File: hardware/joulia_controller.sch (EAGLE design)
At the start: 27 parts, among them IC1 LM2902D, IC2 LM2902D, U1 MMBT2222ALT1G, U2 MMBT2222ALT1G

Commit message: Increasing power trace width and adding input resistors to transistors.
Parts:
- added R16, R9: 1K, resistor:R-US_R0402
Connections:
- new net N$15: R9.1, U1.B
- new net N$16: R16.1, U2.B
- net HEOUT: now also R9.2; no longer U1.B
- net PPOUT: now also R16.2; no longer U2.B
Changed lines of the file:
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@@
 <?xml version="1.0" encoding="utf-8"?>
 <!DOCTYPE eagle SYSTEM "eagle.dtd">
-<eagle version="7.2.0">
+<eagle version="8.0.1">
 <drawing>
 <settings>
@@
 <part name="SUPPLY15" library="supply2" deviceset="GND" device=""/>
 <part name="SUPPLY16" library="supply2" deviceset="GND" device=""/>
+<part name="R9" library="resistor" deviceset="R-US_" device="R0402" value="1K"/>
+<part name="R16" library="resistor" deviceset="R-US_" device="R0402" value="1K"/>
 </parts>
 <sheets>
@@
 <instance part="SUPPLY15" gate="GND" x="50.8" y="81.28"/>
 <instance part="SUPPLY16" gate="GND" x="50.8" y="17.78"/>
+<instance part="R9" gate="G$1" x="190.5" y="109.22" rot="R180"/>
+<instance part="R16" gate="G$1" x="190.5" y="86.36" rot="R180"/>
 </instances>
 <busses>
@@
 <net name="HEOUT" class="0">
 <segment>
-<pinref part="U1" gate="A" pin="B"/>
-<wire x1="198.12" y1="109.22" x2="193.04" y2="109.22" width="0.1524" layer="91"/>
-<label x="193.04" y="109.22" size="1.778" layer="95"/>
-</segment>
-<segment>
 <pinref part="PI" gate="A" pin="13"/>
 <wire x1="-78.74" y1="91.44" x2="-96.52" y2="91.44" width="0.1524" layer="91"/>
 <label x="-96.52" y="91.44" size="1.778" layer="95"/>
 </segment>
+<segment>
+<pinref part="R9" gate="G$1" pin="2"/>
+<label x="180.34" y="109.22" size="1.778" layer="95"/>
+<wire x1="185.42" y1="109.22" x2="180.34" y2="109.22" width="0.1524" layer="91"/>
+</segment>
 </net>
 <net name="PPOUT" class="0">
-<segment>
-<pinref part="U2" gate="A" pin="B"/>
-<wire x1="198.12" y1="86.36" x2="193.04" y2="86.36" width="0.1524" layer="91"/>
-<label x="193.04" y="86.36" size="1.778" layer="95"/>
-</segment>
 <segment>
 <pinref part="PI" gate="A" pin="11"/>
@@
 <label x="-96.52" y="93.98" size="1.778" layer="95"/>
 </segment>
-</net>
+<segment>
+<pinref part="R16" gate="G$1" pin="2"/>
+<label x="180.34" y="86.36" size="1.778" layer="95"/>
+<wire x1="185.42" y1="86.36" x2="180.34" y2="86.36" width="0.1524" layer="91"/>
+</segment>
+</net>
+<net name="N$15" class="0">
+<segment>
+<pinref part="U1" gate="A" pin="B"/>
+<pinref part="R9" gate="G$1" pin="1"/>
+<wire x1="195.58" y1="109.22" x2="198.12" y2="109.22" width="0.1524" layer="91"/>
+</segment>
+</net>
+<net name="N$16" class="0">
+<segment>
+<pinref part="U2" gate="A" pin="B"/>
+<pinref part="R16" gate="G$1" pin="1"/>
+<wire x1="195.58" y1="86.36" x2="198.12" y2="86.36" width="0.1524" layer="91"/>
+</segment>
+</net>

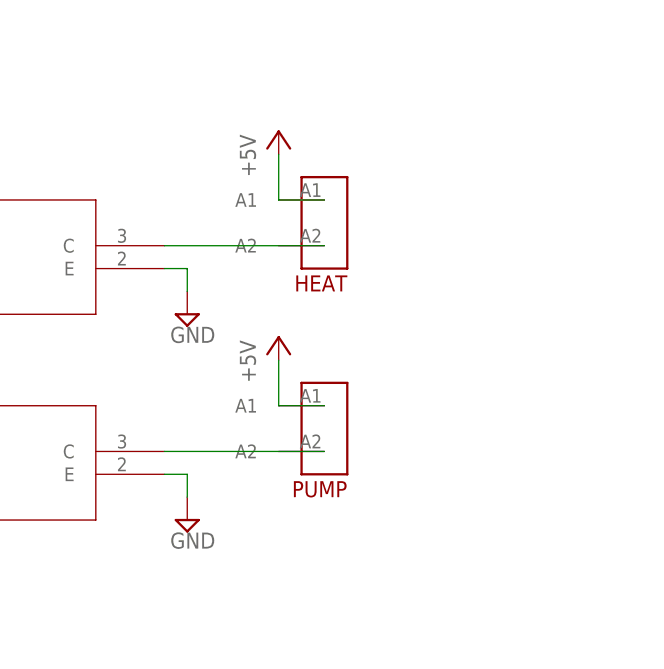
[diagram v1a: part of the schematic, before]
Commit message: Adding Triac and Heatsink
Need opto-isolation and power terminals.
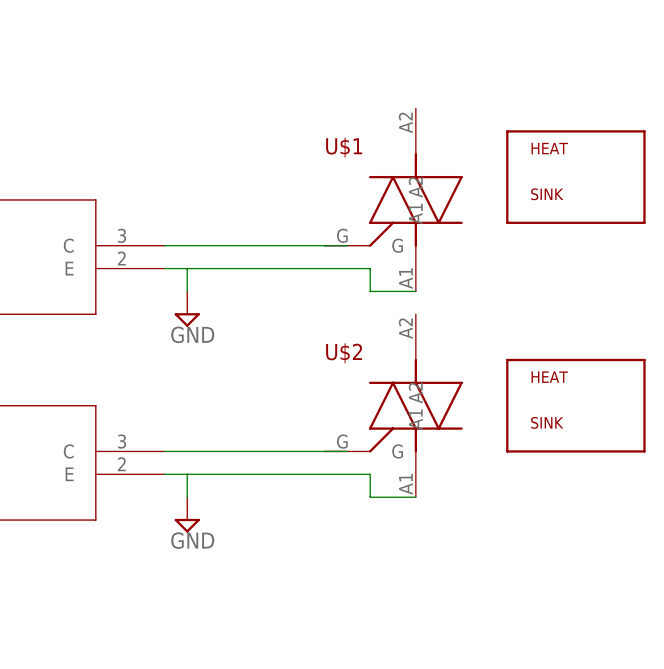
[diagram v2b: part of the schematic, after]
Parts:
- removed HEAT, PUMP: MTA-100-2HDR2, digikey:MTA-100-2HDR2
- added U$1, U$2: T3050H-6I, digikey:T3050H-6I
- added U$3, U$4: VM1-038-1AE, digikey:VM1-038-1AE
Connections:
- net +5V: no longer HEAT.A1, PUMP.A1
- net GND: now also U$1.A1, U$2.A1
- net N$13: now also U$1.G; no longer HEAT.A2
- net N$14: now also U$2.G; no longer PUMP.A2
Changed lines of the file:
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@@
 <part name="U1" library="digikey" deviceset="MMBT2222ALT1G" device=""/>
 <part name="U2" library="digikey" deviceset="MMBT2222ALT1G" device=""/>
-<part name="HEAT" library="digikey" deviceset="MTA-100-2" device="HDR2"/>
-<part name="PUMP" library="digikey" deviceset="MTA-100-2" device="HDR2"/>
-<part name="P+1" library="supply1" deviceset="+5V" device=""/>
-<part name="P+2" library="supply1" deviceset="+5V" device=""/>
 <part name="SUPPLY10" library="supply2" deviceset="GND" device=""/>
 <part name="SUPPLY11" library="supply2" deviceset="GND" device=""/>
@@
 <part name="R9" library="resistor" deviceset="R-US_" device="R0402" value="1K"/>
 <part name="R16" library="resistor" deviceset="R-US_" device="R0402" value="1K"/>
+<part name="U$1" library="digikey" deviceset="T3050H-6I" device=""/>
+<part name="U$2" library="digikey" deviceset="T3050H-6I" device=""/>
+<part name="U$3" library="digikey" deviceset="VM1-038-1AE" device=""/>
+<part name="U$4" library="digikey" deviceset="VM1-038-1AE" device=""/>
 </parts>
 <sheets>
@@
 <instance part="U1" gate="A" x="198.12" y="109.22"/>
 <instance part="U2" gate="A" x="198.12" y="86.36"/>
-<instance part="HEAT" gate="A" x="261.62" y="111.76" rot="MR0"/>
-<instance part="PUMP" gate="A" x="261.62" y="88.9" rot="MR0"/>
-<instance part="P+1" gate="1" x="256.54" y="121.92"/>
-<instance part="P+2" gate="1" x="256.54" y="99.06"/>
 <instance part="SUPPLY10" gate="GND" x="246.38" y="78.74"/>
 <instance part="SUPPLY11" gate="GND" x="246.38" y="101.6"/>
@@
 <instance part="R9" gate="G$1" x="190.5" y="109.22" rot="R180"/>
 <instance part="R16" gate="G$1" x="190.5" y="86.36" rot="R180"/>
+<instance part="U$1" gate="G$1" x="269.24" y="114.3"/>
+<instance part="U$2" gate="G$1" x="269.24" y="91.44"/>
+<instance part="U$3" gate="G$1" x="289.56" y="116.84"/>
+<instance part="U$4" gate="G$1" x="289.56" y="91.44"/>
 </instances>
 <busses>
@@
 <wire x1="243.84" y1="106.68" x2="246.38" y2="106.68" width="0.1524" layer="91"/>
 <wire x1="246.38" y1="106.68" x2="246.38" y2="104.14" width="0.1524" layer="91"/>
+<wire x1="246.38" y1="106.68" x2="266.7" y2="106.68" width="0.1524" layer="91"/>
+<wire x1="266.7" y1="106.68" x2="266.7" y2="104.14" width="0.1524" layer="91"/>
+<pinref part="U$1" gate="G$1" pin="A1"/>
+<wire x1="266.7" y1="104.14" x2="271.78" y2="104.14" width="0.1524" layer="91"/>
 </segment>
 <segment>
@@
 <wire x1="243.84" y1="83.82" x2="246.38" y2="83.82" width="0.1524" layer="91"/>
 <wire x1="246.38" y1="83.82" x2="246.38" y2="81.28" width="0.1524" layer="91"/>
+<wire x1="246.38" y1="83.82" x2="266.7" y2="83.82" width="0.1524" layer="91"/>
+<wire x1="266.7" y1="83.82" x2="266.7" y2="81.28" width="0.1524" layer="91"/>
+<pinref part="U$2" gate="G$1" pin="A1"/>
+<wire x1="266.7" y1="81.28" x2="271.78" y2="81.28" width="0.1524" layer="91"/>
 </segment>
 <segment>
@@
 </segment>
 <segment>
-<pinref part="P+1" gate="1" pin="+5V"/>
-<wire x1="256.54" y1="119.38" x2="256.54" y2="114.3" width="0.1524" layer="91"/>
-<pinref part="HEAT" gate="A" pin="A1"/>
-<wire x1="256.54" y1="114.3" x2="261.62" y2="114.3" width="0.1524" layer="91"/>
-</segment>
-<segment>
-<pinref part="P+2" gate="1" pin="+5V"/>
-<wire x1="256.54" y1="96.52" x2="256.54" y2="91.44" width="0.1524" layer="91"/>
-<pinref part="PUMP" gate="A" pin="A1"/>
-<wire x1="256.54" y1="91.44" x2="261.62" y2="91.44" width="0.1524" layer="91"/>
-</segment>
-<segment>
 <pinref part="P+3" gate="1" pin="+5V"/>
 <wire x1="-71.12" y1="38.1" x2="-71.12" y2="33.02" width="0.1524" layer="91"/>
@@
 <segment>
 <pinref part="U1" gate="A" pin="C"/>
-<wire x1="261.62" y1="109.22" x2="243.84" y2="109.22" width="0.1524" layer="91"/>
-<pinref part="HEAT" gate="A" pin="A2"/>
+<pinref part="U$1" gate="G$1" pin="G"/>
+<wire x1="243.84" y1="109.22" x2="261.62" y2="109.22" width="0.1524" layer="91"/>
+<wire x1="264.16" y1="109.22" x2="261.62" y2="109.22" width="0.1524" layer="91"/>
 </segment>
 </net>
@@
 <segment>
 <pinref part="U2" gate="A" pin="C"/>
+<pinref part="U$2" gate="G$1" pin="G"/>
 <wire x1="243.84" y1="86.36" x2="261.62" y2="86.36" width="0.1524" layer="91"/>
-<pinref part="PUMP" gate="A" pin="A2"/>
-</segment>
-</net>
+<wire x1="264.16" y1="86.36" x2="261.62" y2="86.36" width="0.1524" layer="91"/>
+</segment>
+</net>

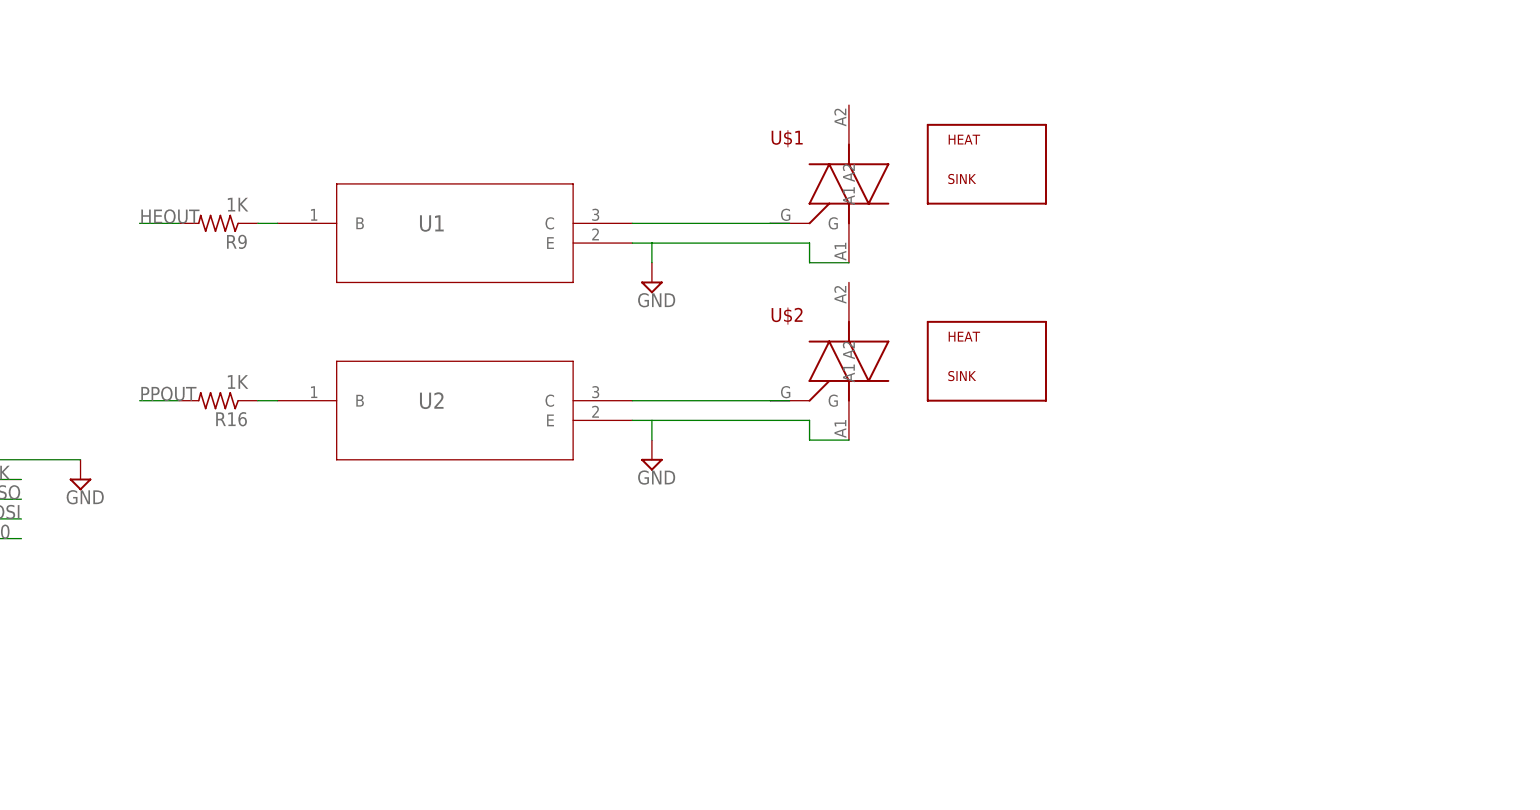
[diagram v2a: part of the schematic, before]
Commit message: Adding connectors and SSR to board
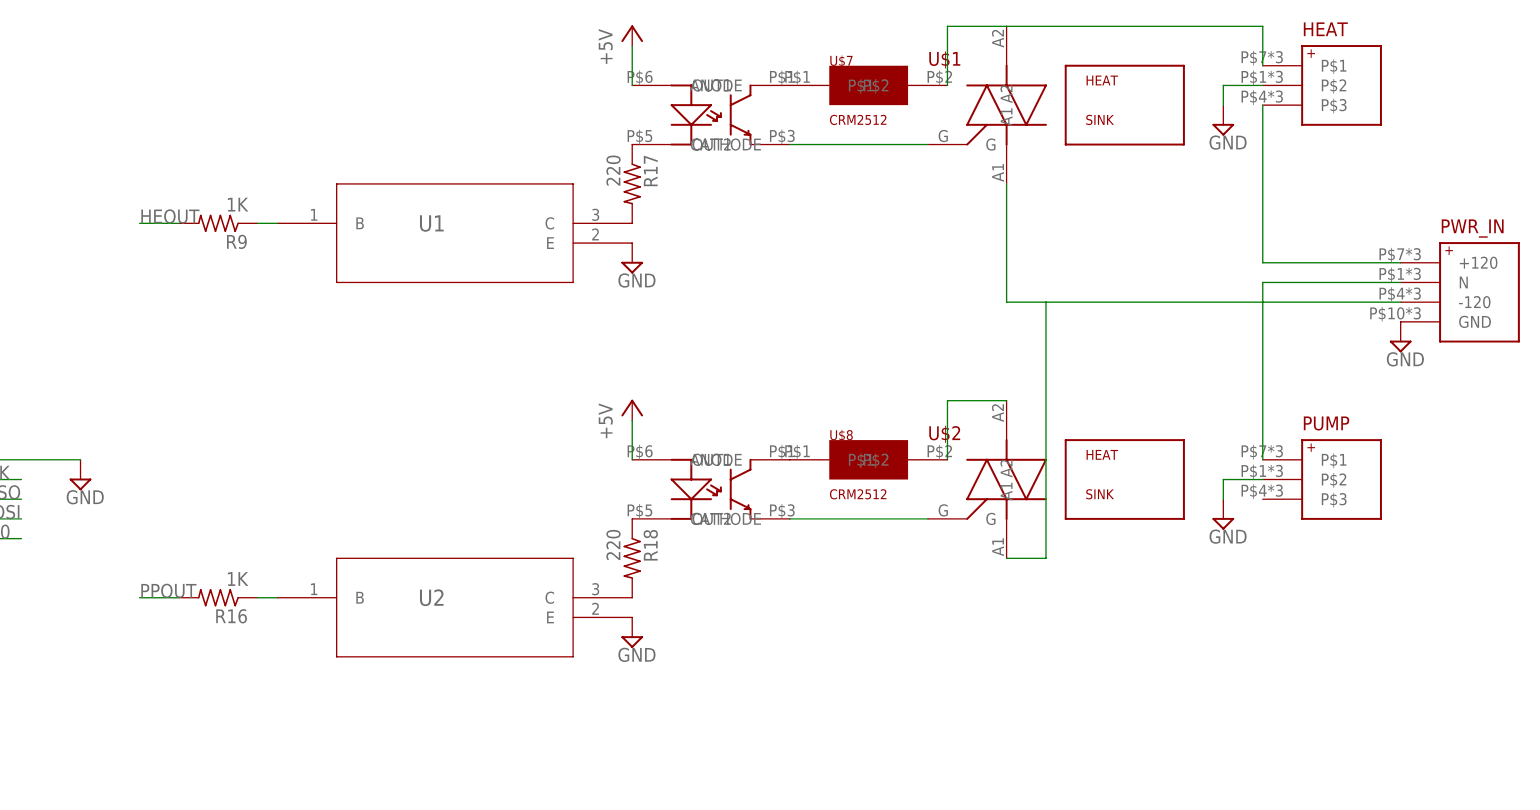
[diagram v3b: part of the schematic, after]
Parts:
- added HEAT, PUMP: PC1720589, digikey:PC1720589
- added PWR_IN: PC1720592, digikey:PC1720592
- added R17, R18: 220, resistor:R-US_R0402
- added U$5, U$6: MOC3020S, digikey:MOC3020S
- added U$7, U$8: CRM2512, digikey:CRM2512
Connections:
- new net N$17: R18.2, U2.C
- new net N$18: R18.1, U$6.CATHODE
- new net N$19: U$1.G, U$5.OUT2
- new net N$20: U$5.OUT1, U$7.P$1
- new net N$21: U$6.OUT1, U$8.P$1
- new net N$22: HEAT.P$1, U$1.A2, U$7.P$2
- new net N$23: U$2.G, U$6.OUT2
- new net N$24: U$2.A2, U$8.P$2
- new net N$25: HEAT.P$3, PWR_IN.+120
- new net N$26: PWR_IN.-120, U$1.A1, U$2.A1
- new net N$27: PUMP.P$1, PWR_IN.N
- net +5V: now also U$5.ANODE, U$6.ANODE
- net GND: now also HEAT.P$2, PUMP.P$2, PWR_IN.GND; no longer U$1.A1, U$2.A1
- net N$13: now also R17.2; no longer U$1.G
- net N$14: now also R17.1, U$5.CATHODE; no longer U$2.G, U2.C
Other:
- moved on the sheet: R16, U$1, U$2, U2

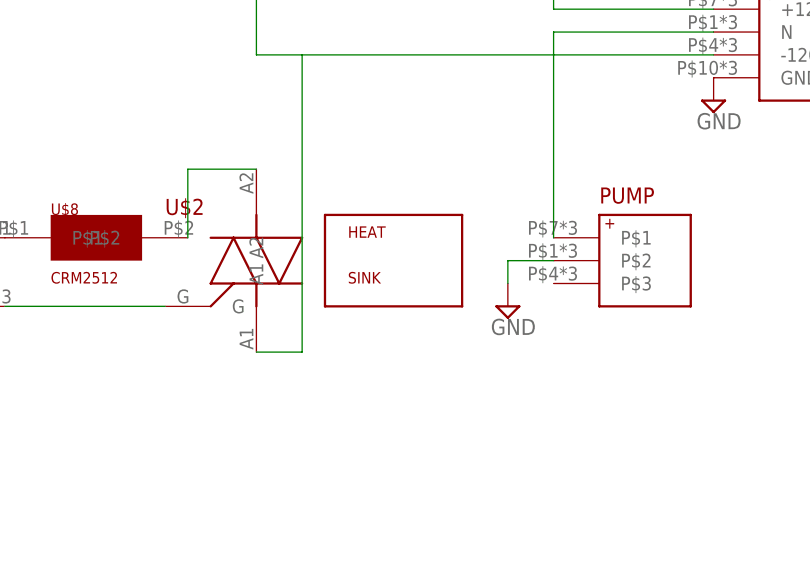
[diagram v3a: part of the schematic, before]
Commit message: Routing and rearrangement for power
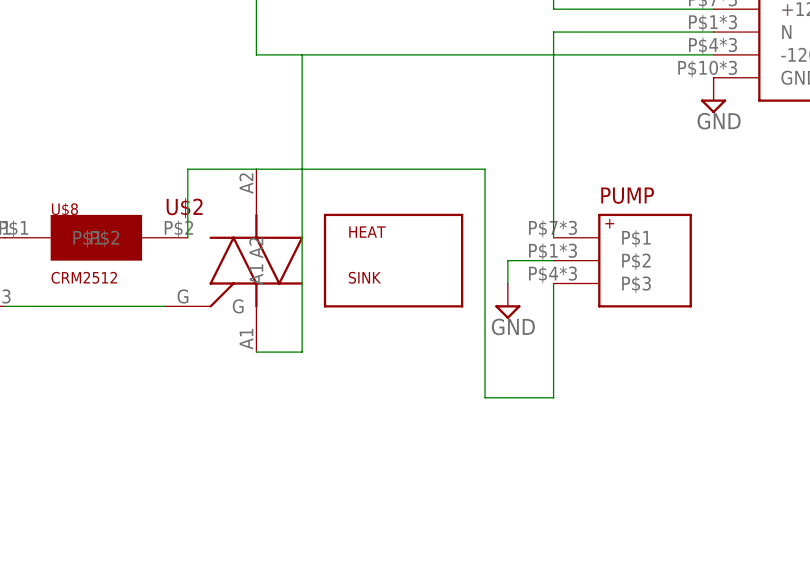
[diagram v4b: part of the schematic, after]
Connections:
- net N$24: now also PUMP.P$3
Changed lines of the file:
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@@
 <pinref part="U$2" gate="G$1" pin="A2"/>
 <wire x1="284.48" y1="86.36" x2="292.1" y2="86.36" width="0.1524" layer="91"/>
+<wire x1="292.1" y1="86.36" x2="317.5" y2="86.36" width="0.1524" layer="91"/>
+<wire x1="317.5" y1="86.36" x2="317.5" y2="60.96" width="0.1524" layer="91"/>
+<pinref part="PUMP" gate="G$1" pin="P$3"/>
+<wire x1="317.5" y1="60.96" x2="325.12" y2="60.96" width="0.1524" layer="91"/>
+<wire x1="325.12" y1="60.96" x2="325.12" y2="73.66" width="0.1524" layer="91"/>
 </segment>
 </net>
